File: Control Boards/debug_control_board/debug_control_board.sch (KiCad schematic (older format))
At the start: 10 parts, among them J1 Conn_01x05, J10 Conn_01x26, J2 Conn_01x05, J3 Conn_01x04, J4 Conn_01x04, J5 Conn_01x05, J6 Conn_01x05, J7 Conn_01x02, J8 Conn_01x03, J9 Conn_01x26

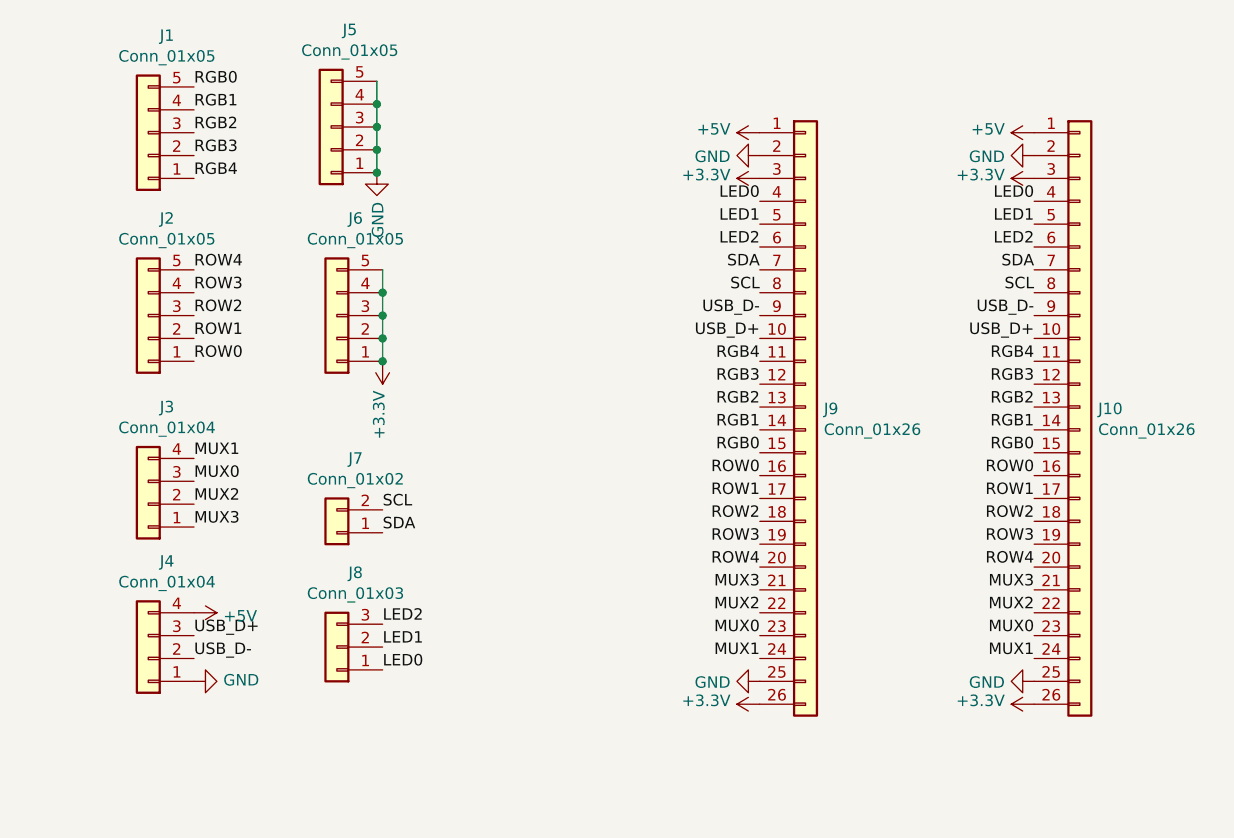
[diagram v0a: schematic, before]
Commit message: Updated debug board to support 30 pin ribbon cable
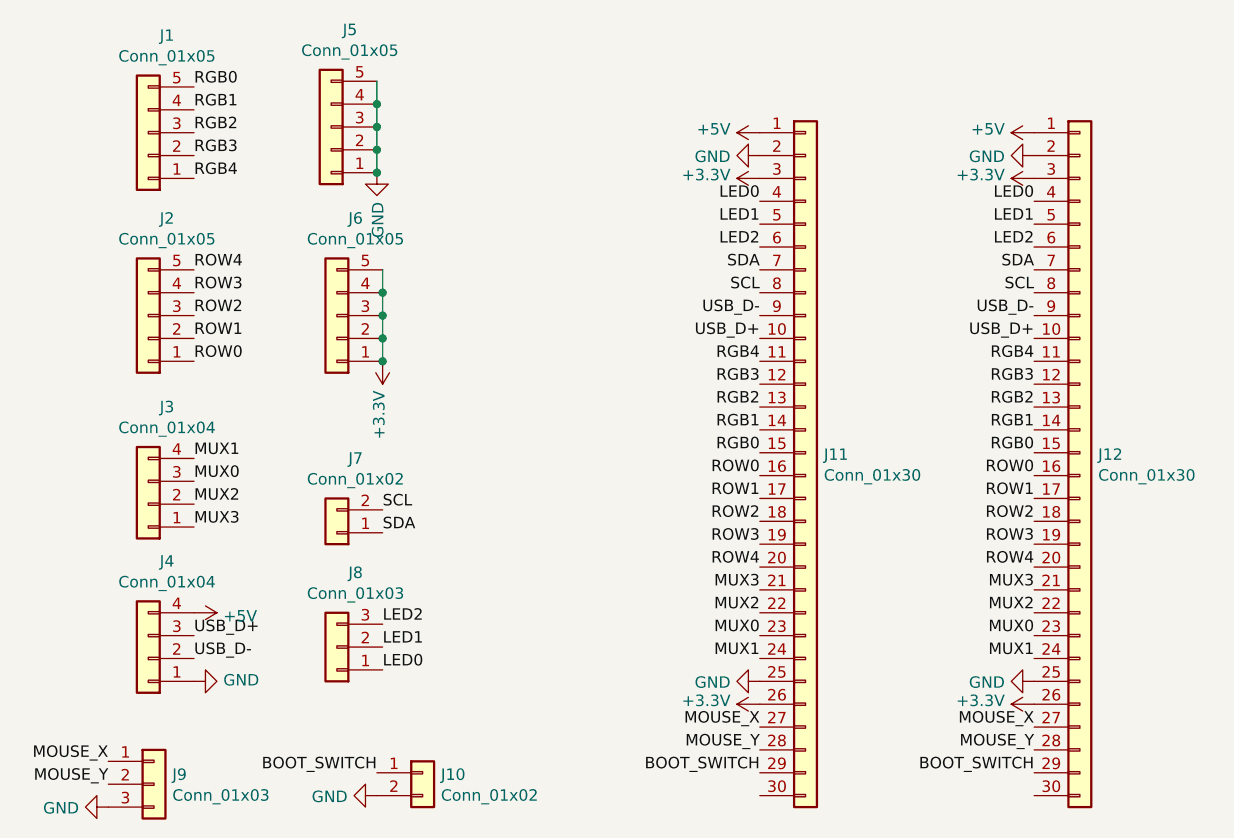
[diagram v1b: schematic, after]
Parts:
- removed J10, J9: Conn_01x26, Connector_FFC-FPC:Hirose_FH12-26S-0.5SH_1x26-1MP_P0.50mm_Horizontal, symbol Connector_Generic:Conn_01x26
- added J10: Conn_01x02, Connector_PinHeader_2.54mm:PinHeader_1x02_P2.54mm_Vertical, symbol Connector_Generic:Conn_01x02
- added J11, J12: Conn_01x30, Connector_FFC-FPC:Hirose_FH12-30S-0.5SH_1x30-1MP_P0.50mm_Horizontal, symbol Connector_Generic:Conn_01x30
- added J9: Conn_01x03, Connector_PinHeader_2.54mm:PinHeader_1x03_P2.54mm_Vertical, symbol Connector_Generic:Conn_01x03
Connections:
- net +3V3: now also J11.26 (Pin_26), J11.3 (Pin_3), J12.26 (Pin_26), J12.3 (Pin_3)
- net +5V: now also J11.1 (Pin_1), J12.1 (Pin_1)
- net GND: now also J10.2 (Pin_2), J11.2 (Pin_2), J11.25 (Pin_25), J12.2 (Pin_2), J12.25 (Pin_25), J9.3 (Pin_3)
- net LED0: now also J11.4 (Pin_4), J12.4 (Pin_4)
- net LED1: now also J11.5 (Pin_5), J12.5 (Pin_5)
- net LED2: now also J11.6 (Pin_6), J12.6 (Pin_6)
- net MUX0: now also J11.23 (Pin_23), J12.23 (Pin_23)
- net MUX1: now also J11.24 (Pin_24), J12.24 (Pin_24)
- net MUX2: now also J11.22 (Pin_22), J12.22 (Pin_22)
- net MUX3: now also J11.21 (Pin_21), J12.21 (Pin_21)
- net RGB0: now also J11.15 (Pin_15), J12.15 (Pin_15)
- net RGB1: now also J11.14 (Pin_14), J12.14 (Pin_14)
- net RGB2: now also J11.13 (Pin_13), J12.13 (Pin_13)
- net RGB3: now also J11.12 (Pin_12), J12.12 (Pin_12)
- net RGB4: now also J11.11 (Pin_11), J12.11 (Pin_11)
- net ROW0: now also J11.16 (Pin_16), J12.16 (Pin_16)
- net ROW1: now also J11.17 (Pin_17), J12.17 (Pin_17)
- net ROW2: now also J11.18 (Pin_18), J12.18 (Pin_18)
- net ROW3: now also J11.19 (Pin_19), J12.19 (Pin_19)
- net ROW4: now also J11.20 (Pin_20), J12.20 (Pin_20)
- net SCL: now also J11.8 (Pin_8), J12.8 (Pin_8)
- net SDA: now also J11.7 (Pin_7), J12.7 (Pin_7)
- net USB_D+: now also J11.10 (Pin_10), J12.10 (Pin_10)
- net USB_D-: now also J11.9 (Pin_9), J12.9 (Pin_9)
- new net BOOT_SWITCH: J10.1 (Pin_1), J11.29 (Pin_29), J12.29 (Pin_29)
- new net MOUSE_X: J11.27 (Pin_27), J12.27 (Pin_27), J9.1 (Pin_1)
- new net MOUSE_Y: J11.28 (Pin_28), J12.28 (Pin_28), J9.2 (Pin_2)
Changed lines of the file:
@@
 $EndDescr
-$Comp
-L Connector_Generic:Conn_01x26 J9
-U 1 1 6198690D
-P 6225 3950
-F 0 "J9" H 6305 3942 50  0000 L CNN
-F 1 "Conn_01x26" H 6305 3851 50  0000 L CNN
-F 2 "Connector_FFC-FPC:Hirose_FH12-26S-0.5SH_1x26-1MP_P0.50mm_Horizontal" H 6225 3950 50  0001 C CNN
-F 3 "~" H 6225 3950 50  0001 C CNN
-	1    6225 3950
-	1    0    0    -1
-$EndComp
 $Comp
 L power:+5V #PWR0101
@@
 MUX1
 $Comp
-L Connector_Generic:Conn_01x26 J10
-U 1 1 5E8E9B0F
-P 7425 3950
-F 0 "J10" H 7505 3942 50  0000 L CNN
-F 1 "Conn_01x26" H 7505 3851 50  0000 L CNN
-F 2 "Connector_FFC-FPC:Hirose_FH12-26S-0.5SH_1x26-1MP_P0.50mm_Horizontal" H 7425 3950 50  0001 C CNN
-F 3 "~" H 7425 3950 50  0001 C CNN
-	1    7425 3950
-	1    0    0    -1
-$EndComp
-$Comp
 L power:+5V #PWR0106
 U 1 1 5E8E9B19
@@
 Text Label 4375 4900 0    50   ~ 0
 LED2
+$Comp
+L Connector_Generic:Conn_01x30 J11
+U 1 1 5EA08939
+P 6225 4150
+F 0 "J11" H 6305 4142 50  0000 L CNN
+F 1 "Conn_01x30" H 6305 4051 50  0000 L CNN
+F 2 "Connector_FFC-FPC:Hirose_FH12-30S-0.5SH_1x30-1MP_P0.50mm_Horizontal" H 6225 4150 50  0001 C CNN
+F 3 "~" H 6225 4150 50  0001 C CNN
+	1    6225 4150
+	1    0    0    -1
+$EndComp
+$Comp
+L Connector_Generic:Conn_01x30 J12
+U 1 1 5EA09A24
+P 7425 4150
+F 0 "J12" H 7505 4142 50  0000 L CNN
+F 1 "Conn_01x30" H 7505 4051 50  0000 L CNN
+F 2 "Connector_FFC-FPC:Hirose_FH12-30S-0.5SH_1x30-1MP_P0.50mm_Horizontal" H 7425 4150 50  0001 C CNN
+F 3 "~" H 7425 4150 50  0001 C CNN
+	1    7425 4150
+	1    0    0    -1
+$EndComp
+Text Label 6025 5350 2    50   ~ 0
+MOUSE_X
+Text Label 7225 5350 2    50   ~ 0
+MOUSE_X
+Text Label 7225 5450 2    50   ~ 0
+MOUSE_Y
+Text Label 6025 5450 2    50   ~ 0
+MOUSE_Y
+Text Label 6025 5550 2    50   ~ 0
+BOOT_SWITCH
+Text Label 7225 5550 2    50   ~ 0
+BOOT_SWITCH
+$Comp
+L Connector_Generic:Conn_01x03 J9
+U 1 1 5EA13C5A
+P 3375 5600
+F 0 "J9" H 3455 5642 50  0000 L CNN
+F 1 "Conn_01x03" H 3455 5551 50  0000 L CNN
+F 2 "Connector_PinHeader_2.54mm:PinHeader_1x03_P2.54mm_Vertical" H 3375 5600 50  0001 C CNN
+F 3 "~" H 3375 5600 50  0001 C CNN
+	1    3375 5600
+	1    0    0    -1
+$EndComp
+$Comp
+L Connector_Generic:Conn_01x02 J10
+U 1 1 5EA1451B
+P 4550 5550
+F 0 "J10" H 4630 5542 50  0000 L CNN
+F 1 "Conn_01x02" H 4630 5451 50  0000 L CNN
+F 2 "Connector_PinHeader_2.54mm:PinHeader_1x02_P2.54mm_Vertical" H 4550 5550 50  0001 C CNN
+F 3 "~" H 4550 5550 50  0001 C CNN
+	1    4550 5550
+	1    0    0    -1
+$EndComp
+$Comp
+L power:GND #PWR0115
+U 1 1 5EA14DDB
+P 3175 5700
+F 0 "#PWR0115" H 3175 5450 50  0001 C CNN
+F 1 "GND" V 3180 5572 50  0000 R CNN
+F 2 "" H 3175 5700 50  0001 C CNN
+F 3 "" H 3175 5700 50  0001 C CNN
+	1    3175 5700
+	0    1    1    0
+$EndComp
+$Comp
+L power:GND #PWR0116
+U 1 1 5EA152DE
+P 4350 5650
+F 0 "#PWR0116" H 4350 5400 50  0001 C CNN
+F 1 "GND" V 4355 5522 50  0000 R CNN
+F 2 "" H 4350 5650 50  0001 C CNN
+F 3 "" H 4350 5650 50  0001 C CNN
+	1    4350 5650
+	0    1    1    0
+$EndComp
+Text Label 3175 5600 2    50   ~ 0
+MOUSE_Y
+Text Label 3175 5500 2    50   ~ 0
+MOUSE_X
+Text Label 4350 5550 2    50   ~ 0
+BOOT_SWITCH
 $EndSCHEMATC
